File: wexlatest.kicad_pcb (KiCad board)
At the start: 2 copper layers, 86 x 100 mm, 58 parts, among them J1 Screw_Terminal_01x02, J2 Conn_02x10_Odd_Even, J3 DB25_Female, J5 Conn_02x06_Odd_Even, SW10 SW_DIP_x06, SW5 SW_DIP_x01

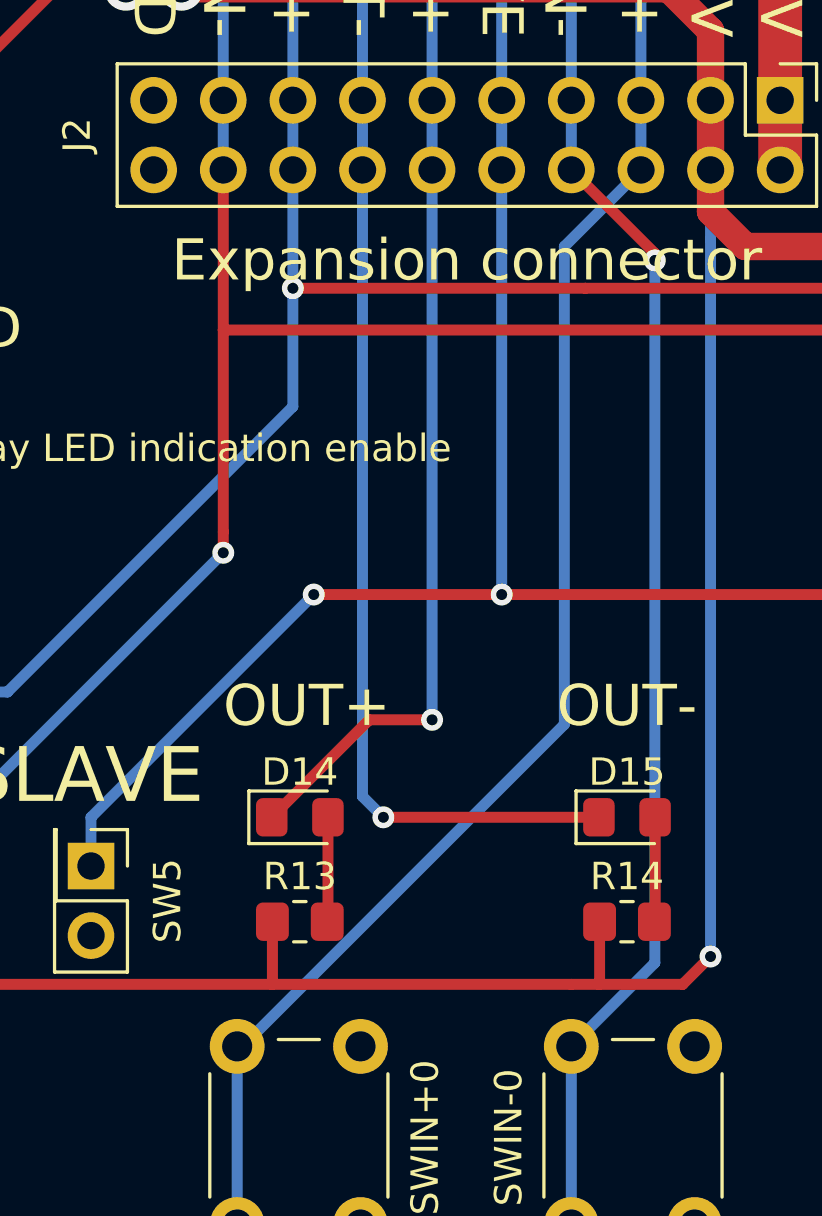
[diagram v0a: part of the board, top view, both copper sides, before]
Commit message: Enlange filled zone.
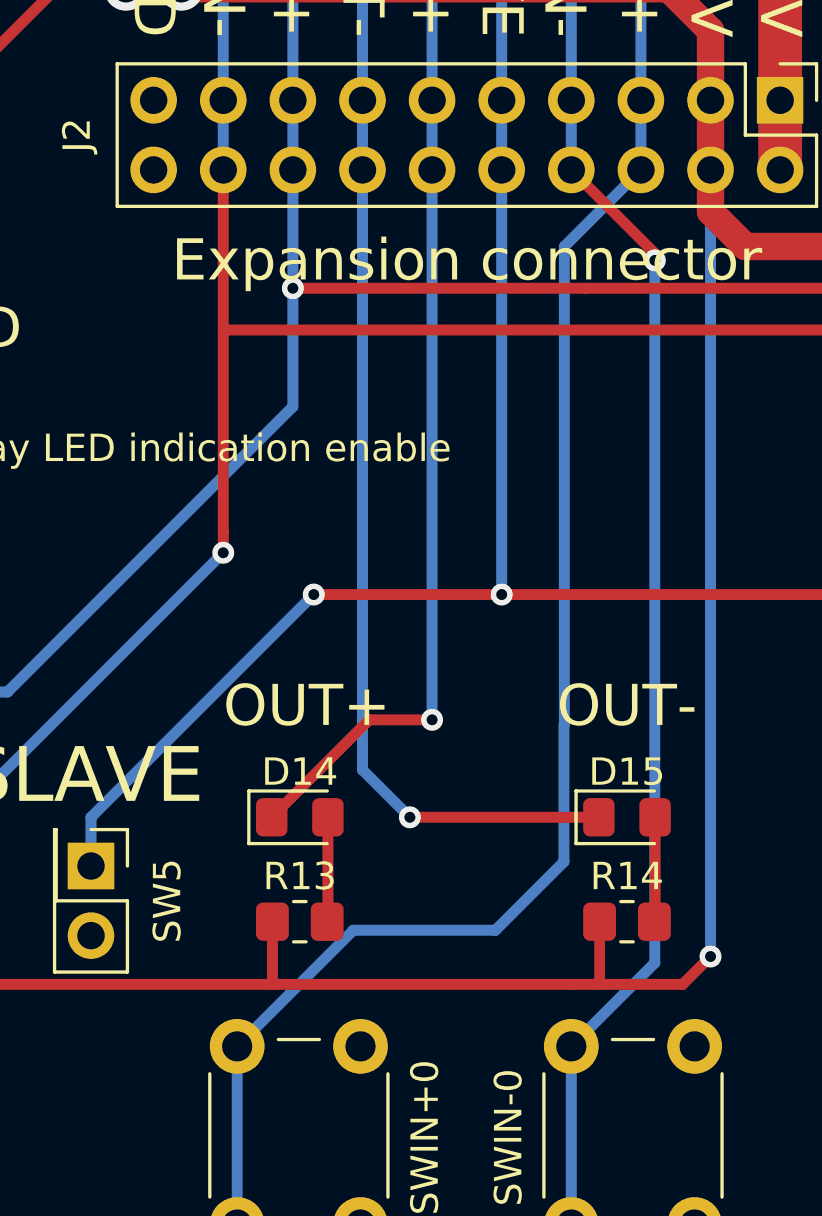
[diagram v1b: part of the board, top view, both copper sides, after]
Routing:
- net IN+: track 94.3 -> 97.4 mm
- net OUT-: track 56.3 -> 55.7 mm

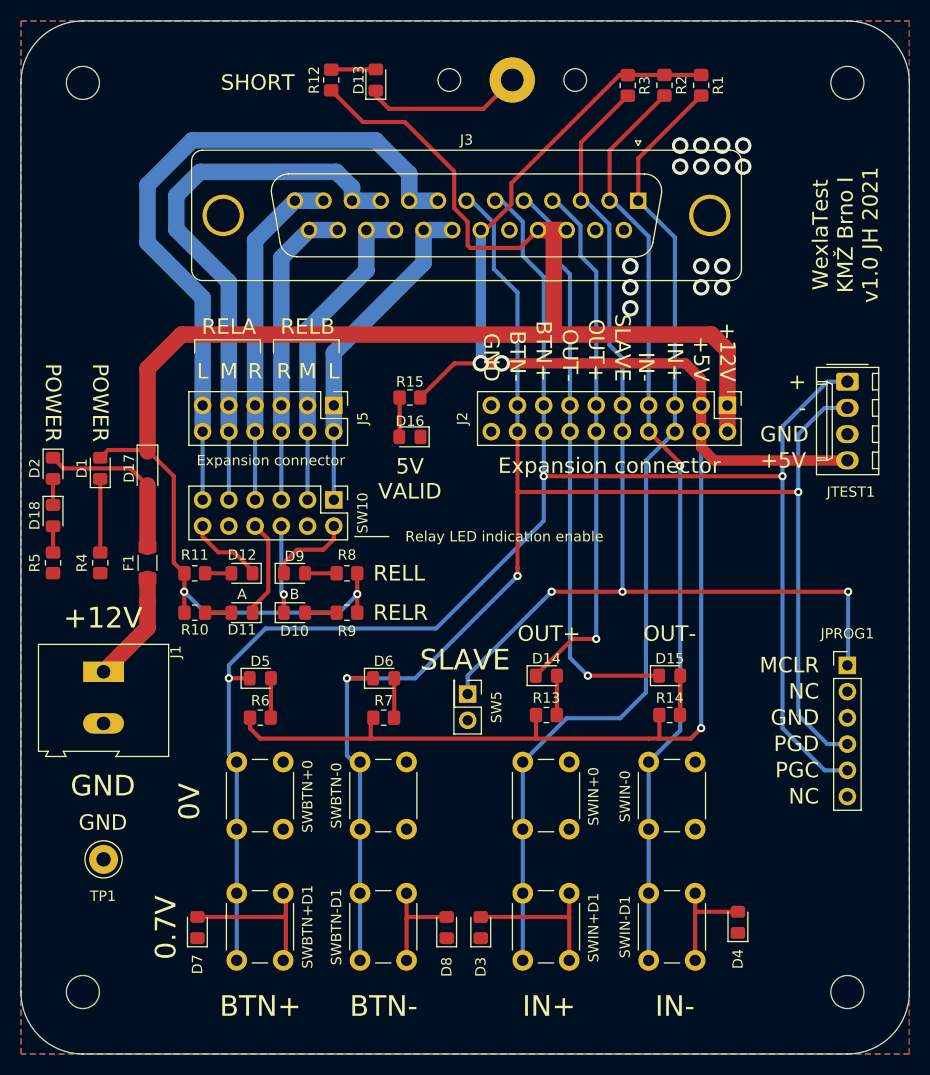
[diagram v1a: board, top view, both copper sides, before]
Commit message: Fix bad relay polarity.
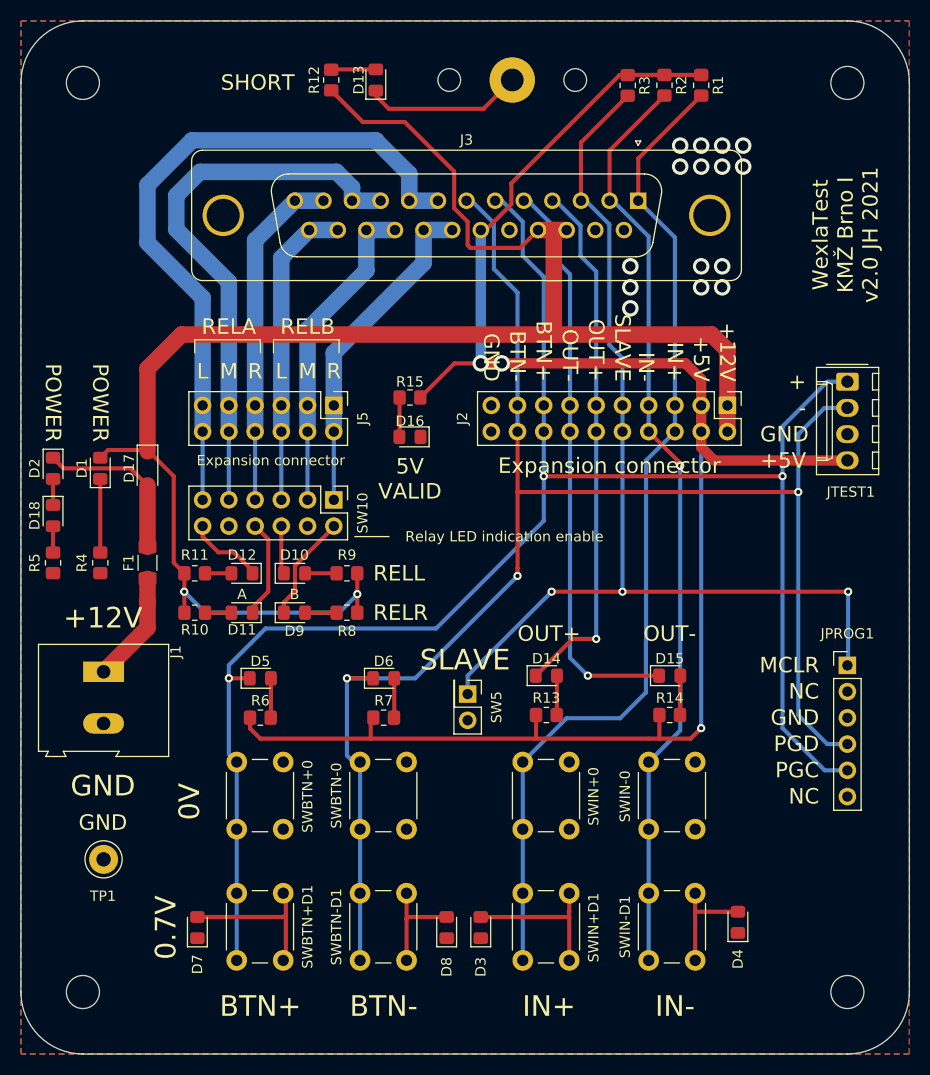
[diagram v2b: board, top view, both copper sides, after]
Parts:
- moved D10 3.81 mm to (141.5, 93.5)
- moved D9 3.81 mm to (141.5, 97.3)
- moved R8 3.81 mm to (146.6, 97.3)
- moved R9 3.81 mm to (146.6, 93.5)
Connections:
- J3 pad 20: RELBL -> RELBR
- J3 pad 21: RELBL -> RELBR
- J3 pad 24: RELBR -> RELBL
- J3 pad 25: RELBR -> RELBL
- J5 pad 1: RELBL -> RELBR
- J5 pad 2: RELBL -> RELBR
- J5 pad 5: RELBR -> RELBL
- J5 pad 6: RELBR -> RELBL
- SW10 pad 1: RELBL -> RELBR
- SW10 pad 5: RELBR -> RELBL
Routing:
- net Net-(D10-Pad1): track 8.48 -> 4.67 mm, vias 1 -> 0
- net RELBR: track 30.0 -> 32.5 mm
- net RELBL: track 32.5 -> 30.0 mm
- net Net-(D9-Pad1): track 8.06 -> 10.4 mm
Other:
- board text added: "WexlaTest KMŽ Brno I v2.0 JH 2021"
- board text removed: "WexlaTest KMŽ Brno I v1.0 JH 2021"

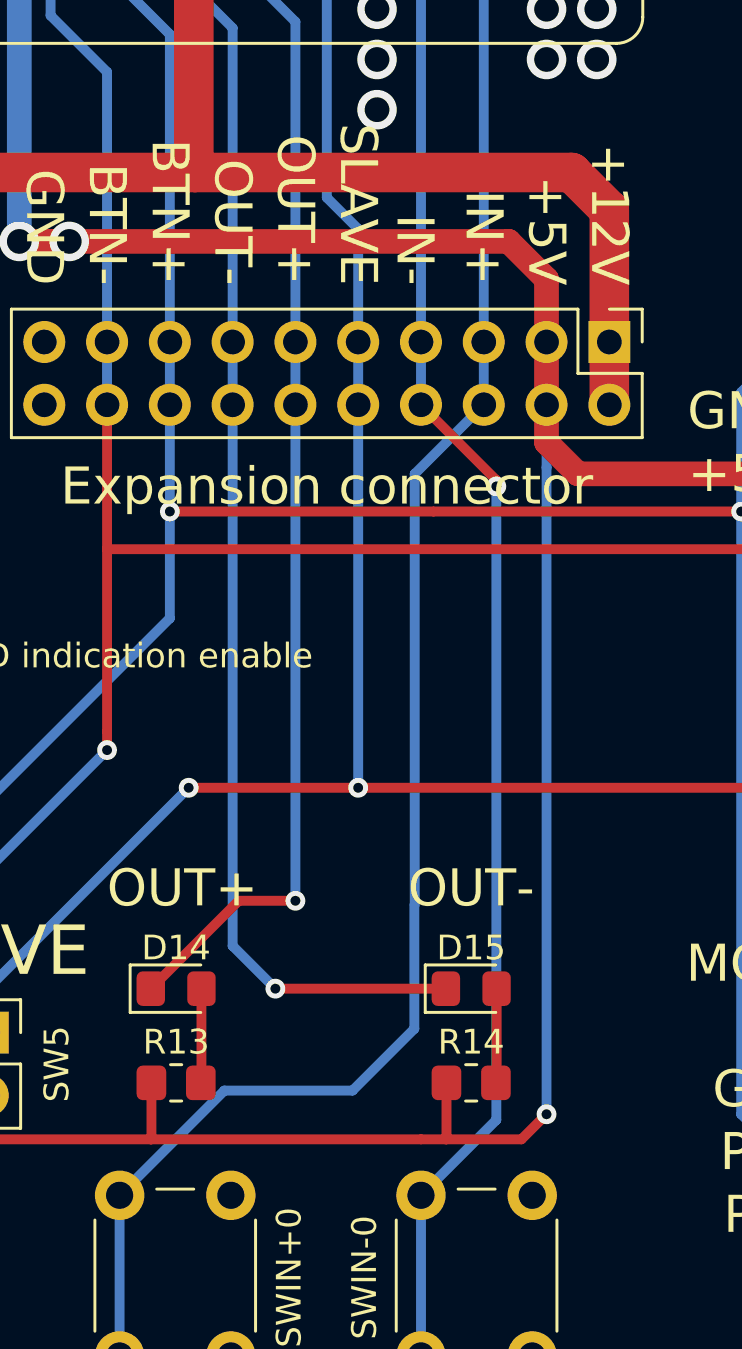
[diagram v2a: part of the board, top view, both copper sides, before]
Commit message: Fix switched OUT+ & OUT-.
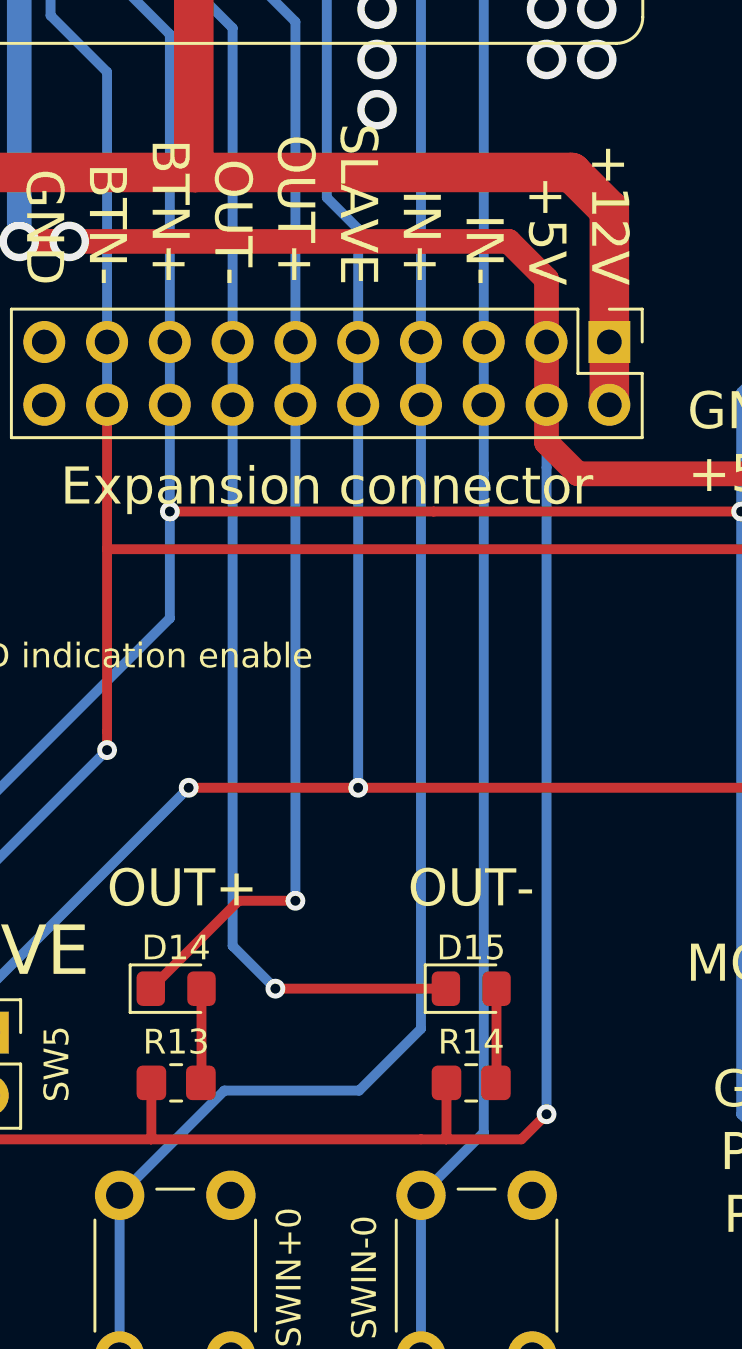
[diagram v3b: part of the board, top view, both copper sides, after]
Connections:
- J2 pad 5: IN+ -> IN-
- J2 pad 6: IN+ -> IN-
- J2 pad 7: IN- -> IN+
- J2 pad 8: IN- -> IN+
- J3 pad 1: IN+ -> IN-
- J3 pad 2: IN- -> IN+
- R1 pad 2: IN+ -> IN-
- R2 pad 2: IN- -> IN+
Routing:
- net IN-: track 90.4 -> 88.8 mm, vias 1 -> 0
- net IN+: track 97.4 -> 96.8 mm
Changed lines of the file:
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@@
     (thickness 1.6)
     (drawings 84)
-    (tracks 337)
+    (tracks 335)
     (zones 0)
     (modules 58)
@@
     )
     (pad 2 smd roundrect (at 1 0 270) (size 1.2 1.4) (layers F.Cu F.Paste F.Mask) (roundrect_rratio 0.208333)
-      (net 28 IN-))
+      (net 29 IN+))
     (pad 1 smd roundrect (at -1 0 270) (size 1.2 1.4) (layers F.Cu F.Paste F.Mask) (roundrect_rratio 0.208333)
       (net 30 +5V))
@@
     )
     (pad 2 smd roundrect (at 1 0 270) (size 1.2 1.4) (layers F.Cu F.Paste F.Mask) (roundrect_rratio 0.208333)
-      (net 29 IN+))
+      (net 28 IN-))
     (pad 1 smd roundrect (at -1 0 270) (size 1.2 1.4) (layers F.Cu F.Paste F.Mask) (roundrect_rratio 0.208333)
       (net 30 +5V))
@@
       (net 27 IN-SLAVE|MCLR))
     (pad 2 thru_hole circle (at -2.77 0) (size 1.6 1.6) (drill 1) (layers *.Cu *.Mask)
+      (net 29 IN+))
+    (pad 1 thru_hole rect (at 0 0) (size 1.6 1.6) (drill 1) (layers *.Cu *.Mask)
       (net 28 IN-))
-    (pad 1 thru_hole rect (at 0 0) (size 1.6 1.6) (drill 1) (layers *.Cu *.Mask)
-      (net 29 IN+))
     (model ${KISYS3DMOD}/Connector_Dsub.3dshapes/DSUB-25_Female_Vertical_P2.77x2.84mm_MountingHoles.wrl
       (at (xyz 0 0 0))
@@
       (net 27 IN-SLAVE|MCLR))
     (pad 8 thru_hole oval (at 2.54 7.62 270) (size 1.7 1.7) (drill 1) (layers *.Cu *.Mask)
+      (net 29 IN+))
+    (pad 7 thru_hole oval (at 0 7.62 270) (size 1.7 1.7) (drill 1) (layers *.Cu *.Mask)
+      (net 29 IN+))
+    (pad 6 thru_hole oval (at 2.54 5.08 270) (size 1.7 1.7) (drill 1) (layers *.Cu *.Mask)
       (net 28 IN-))
-    (pad 7 thru_hole oval (at 0 7.62 270) (size 1.7 1.7) (drill 1) (layers *.Cu *.Mask)
+    (pad 5 thru_hole oval (at 0 5.08 270) (size 1.7 1.7) (drill 1) (layers *.Cu *.Mask)
       (net 28 IN-))
-    (pad 6 thru_hole oval (at 2.54 5.08 270) (size 1.7 1.7) (drill 1) (layers *.Cu *.Mask)
-      (net 29 IN+))
-    (pad 5 thru_hole oval (at 0 5.08 270) (size 1.7 1.7) (drill 1) (layers *.Cu *.Mask)
-      (net 29 IN+))
     (pad 4 thru_hole oval (at 2.54 2.54 270) (size 1.7 1.7) (drill 1) (layers *.Cu *.Mask)
       (net 30 +5V))
@@
     (effects (font (size 1.5 1.5) (thickness 0.15)) (justify right))
   )
-  (gr_text IN- (at 175.514 74.93 -90) (layer F.SilkS)
+  (gr_text IN- (at 178.308 74.93 -90) (layer F.SilkS)
     (effects (font (size 1.5 1.5) (thickness 0.15)) (justify right))
   )
-  (gr_text IN+ (at 178.308 74.93 270) (layer F.SilkS)
+  (gr_text IN+ (at 175.768 74.93 270) (layer F.SilkS)
     (effects (font (size 1.5 1.5) (thickness 0.15)) (justify right))
   )
@@
   (segment (start 169.212 51.768) (end 173.736 47.244) (width 0.4) (layer F.Cu) (net 27))
   (segment (start 169.212 57.404) (end 169.212 51.768) (width 0.4) (layer F.Cu) (net 27))
-  (segment (start 175.768 60.868998) (end 175.768 77.216) (width 0.4) (layer B.Cu) (net 28))
-  (segment (start 172.303002 57.404) (end 175.768 60.868998) (width 0.4) (layer B.Cu) (net 28))
-  (segment (start 171.982 57.404) (end 172.303002 57.404) (width 0.4) (layer B.Cu) (net 28))
-  (segment (start 175.768 77.216) (end 175.768 79.756) (width 0.4) (layer B.Cu) (net 28))
-  (segment (start 177.292 47.038) (end 177.292 47.228) (width 0.4) (layer F.Cu) (net 28))
-  (segment (start 177.316 47.014) (end 177.292 47.038) (width 0.4) (layer F.Cu) (net 28))
+  (segment (start 175.768 60.868998) (end 175.768 77.216) (width 0.4) (layer B.Cu) (net 29))
+  (segment (start 172.303002 57.404) (end 175.768 60.868998) (width 0.4) (layer B.Cu) (net 29))
+  (segment (start 171.982 57.404) (end 172.303002 57.404) (width 0.4) (layer B.Cu) (net 29))
+  (segment (start 175.768 77.216) (end 175.768 79.756) (width 0.4) (layer B.Cu) (net 29))
+  (segment (start 177.292 47.038) (end 177.292 47.228) (width 0.4) (layer F.Cu) (net 29))
+  (segment (start 177.316 47.014) (end 177.292 47.038) (width 0.4) (layer F.Cu) (net 29))
   (segment (start 175.768 130.937) (end 175.768 124.437) (width 0.4) (layer B.Cu) (net 28))
   (segment (start 175.768 118.237) (end 175.768 111.737) (width 0.4) (layer B.Cu) (net 28))
   (segment (start 175.768 124.437) (end 175.768 118.237) (width 0.4) (layer B.Cu) (net 28))
-  (via (at 178.816 83.058) (size 0.8) (drill 0.4) (layers F.Cu B.Cu) (net 28))
-  (segment (start 175.768 79.756) (end 178.816 82.804) (width 0.4) (layer F.Cu) (net 28))
-  (segment (start 178.816 82.804) (end 178.816 83.058) (width 0.4) (layer F.Cu) (net 28))
-  (segment (start 175.768 111.737) (end 178.816 108.689) (width 0.4) (layer B.Cu) (net 28))
-  (segment (start 178.816 108.689) (end 178.816 83.058) (width 0.4) (layer B.Cu) (net 28))
-  (segment (start 171.982 52.538) (end 177.292 47.228) (width 0.4) (layer F.Cu) (net 28))
-  (segment (start 171.982 57.404) (end 171.982 52.538) (width 0.4) (layer F.Cu) (net 28))
-  (segment (start 178.308 60.96) (end 178.308 77.216) (width 0.4) (layer B.Cu) (net 29))
-  (segment (start 174.752 57.404) (end 178.308 60.96) (width 0.4) (layer B.Cu) (net 29))
-  (segment (start 178.308 79.756) (end 178.308 77.216) (width 0.4) (layer B.Cu) (net 29))
+  (segment (start 171.982 52.538) (end 177.292 47.228) (width 0.4) (layer F.Cu) (net 29))
+  (segment (start 171.982 57.404) (end 171.982 52.538) (width 0.4) (layer F.Cu) (net 29))
+  (segment (start 178.308 60.96) (end 178.308 77.216) (width 0.4) (layer B.Cu) (net 28))
+  (segment (start 174.752 57.404) (end 178.308 60.96) (width 0.4) (layer B.Cu) (net 28))
+  (segment (start 178.308 79.756) (end 178.308 77.216) (width 0.4) (layer B.Cu) (net 28))
   (segment (start 163.576 118.491) (end 163.322 118.237) (width 0.4) (layer F.Cu) (net 29))
   (segment (start 163.576 130.937) (end 163.576 124.437) (width 0.4) (layer B.Cu) (net 29))
@@
   (segment (start 163.576 118.237) (end 163.576 111.737) (width 0.4) (layer B.Cu) (net 29))
   (segment (start 163.767002 111.737) (end 163.576 111.737) (width 0.4) (layer B.Cu) (net 29))
-  (segment (start 175.514 82.55) (end 175.514 99.990002) (width 0.4) (layer B.Cu) (net 29))
-  (segment (start 178.308 79.756) (end 175.514 82.55) (width 0.4) (layer B.Cu) (net 29))
-  (segment (start 174.752 53.324) (end 180.848 47.228) (width 0.4) (layer F.Cu) (net 29))
-  (segment (start 174.752 57.404) (end 174.752 53.324) (width 0.4) (layer F.Cu) (net 29))
+  (segment (start 174.752 53.324) (end 180.848 47.228) (width 0.4) (layer F.Cu) (net 28))
+  (segment (start 174.752 57.404) (end 174.752 53.324) (width 0.4) (layer F.Cu) (net 28))
+  (segment (start 178.308 82.55) (end 178.308 79.756) (width 0.4) (layer B.Cu) (net 28))
+  (segment (start 178.308 109.197) (end 178.308 82.55) (width 0.4) (layer B.Cu) (net 28))
+  (segment (start 175.768 111.737) (end 178.308 109.197) (width 0.4) (layer B.Cu) (net 28))
+  (segment (start 175.514 80.01) (end 175.768 79.756) (width 0.4) (layer B.Cu) (net 29))
+  (segment (start 175.768 99.990002) (end 175.768 80.01) (width 0.4) (layer B.Cu) (net 29))
+  (segment (start 175.768 105) (end 175.768 100) (width 0.4) (layer B.Cu) (net 29))
+  (segment (start 173.268 107.5) (end 175.768 105) (width 0.4) (layer B.Cu) (net 29))
+  (segment (start 167.813 107.5) (end 173.268 107.5) (width 0.4) (layer B.Cu) (net 29))
   (segment (start 163.576 111.737) (end 167.813 107.5) (width 0.4) (layer B.Cu) (net 29))
-  (segment (start 167.813 107.5) (end 173 107.5) (width 0.4) (layer B.Cu) (net 29))
-  (segment (start 173 107.5) (end 175.5 105) (width 0.4) (layer B.Cu) (net 29))
-  (segment (start 175.5 105) (end 175.5 100) (width 0.4) (layer B.Cu) (net 29))
   (segment (start 159.517 60.244) (end 159.517 73.147) (width 1) (layer B.Cu) (net 30))
   (segment (start 159.517 73.147) (end 159.512 73.152) (width 1) (layer B.Cu) (net 30))
